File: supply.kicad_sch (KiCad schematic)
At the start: 39 parts, among them IC3 TPS259571DSGR, IC4 BQ27427YZFR, IC4 TPD6E001RSERG4, IC5 MP2722GRH-0000-Z, IC6 TPS62291DRVR, IC7 TPS62293DRVR, J4 UJ20-C-V-SMT-TR-68, J5 SM03B-SRSS-TB_LF__SN_

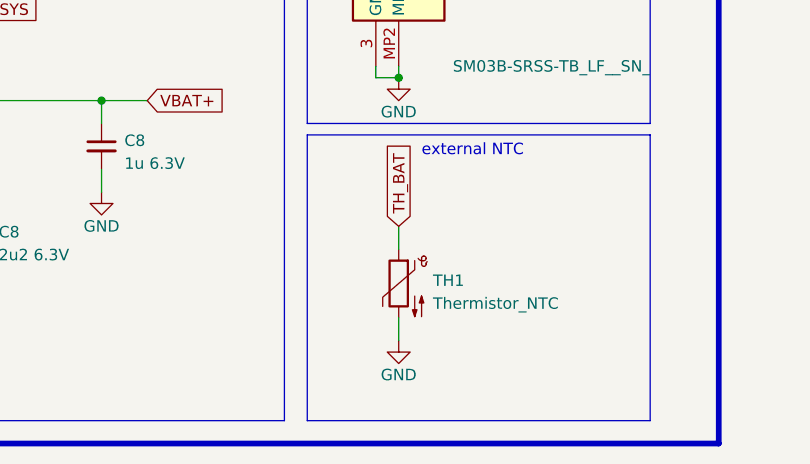
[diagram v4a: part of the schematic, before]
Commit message: first layout iteration
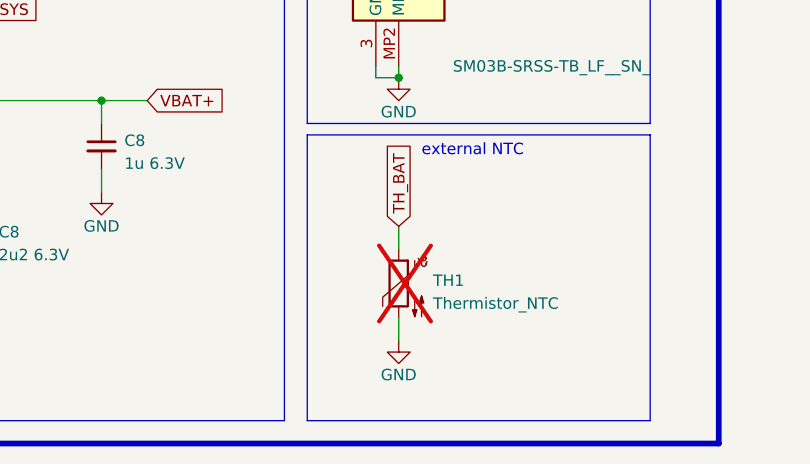
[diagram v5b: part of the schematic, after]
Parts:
- R2: footprint Resistor_SMD:R_0201_0603Metric_Pad0.64x0.40mm_HandSolder -> Resistor_SMD:R_0201_0603Metric
- TH1: now not fitted
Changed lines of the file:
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@@
       (effects (font (size 1.27 1.27)) (justify right))
     )
-    (property "Footprint" "Resistor_SMD:R_0201_0603Metric_Pad0.64x0.40mm_HandSolder" (at 180.34 165.1 0)
+    (property "Footprint" "Resistor_SMD:R_0201_0603Metric" (at 180.34 165.1 0)
       (effects (font (size 1.27 1.27)) hide)
     )
@@
   )
   (symbol (lib_id "Device:Thermistor_NTC") (at 259.08 259.08 0) (mirror y) (unit 1)
-    (in_bom yes) (on_board yes) (dnp no)
+    (in_bom yes) (on_board no) (dnp yes)
     (property "Reference" "TH1" (at 262.89 258.7625 0)
       (effects (font (size 1.27 1.27)) (justify right))

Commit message: progressed layout, adjusted some courtyard sized to be smaller
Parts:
- IC4: Manufacturer_Name (none) -> Texas Instruments; Manufacturer_Part_Number (none) -> TPD6E001RSERG4; Mouser Part Number (none) -> 595-TPD6E001RSERG4; Mouser Price/Stock (none) -> https://www.mouser.co.uk/ProductDetail/Texas-Instruments/TP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
- J4: Manufacturer_Name (none) -> CUI Devices; Manufacturer_Part_Number (none) -> UJ20-C-V-SMT-TR-68; Mouser Part Number (none) -> 179-UJ20-C-V-SMTTR68; Mouser Price/Stock (none) -> https://www.mouser.co.uk/ProductDetail/CUI-Devices/UJ20-C-V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
- R3: footprint Resistor_SMD:R_0201_0603Metric_Pad0.64x0.40mm_HandSolder -> Resistor_SMD:R_0201_0603Metric
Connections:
- net EP: now also J4.B12 (GND_4)
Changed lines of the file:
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@@
       (effects (font (size 1.27 1.27)) (justify right))
     )
-    (property "Footprint" "Resistor_SMD:R_0201_0603Metric_Pad0.64x0.40mm_HandSolder" (at 240.03 40.64 0)
+    (property "Footprint" "Resistor_SMD:R_0201_0603Metric" (at 240.03 40.64 0)
       (effects (font (size 1.27 1.27)) hide)
     )
@@
     (property "MFN" "179-UJ20-C-V-SMTTR68" (at 55.88 46.99 0)
       (effects (font (size 1.27 1.27)) hide)
+    )
+    (property "Mouser Part Number" "179-UJ20-C-V-SMTTR68" (at 26.67 541.91 0)
+      (effects (font (size 1.27 1.27)) (justify left top) hide)
+    )
+    (property "Mouser Price/Stock" "https://www.mouser.co.uk/ProductDetail/CUI-Devices/UJ20-C-V-SMT-TR-68?qs=HoCaDK9Nz5dJB%252B3Mk1F%2F5A%3D%3D" (at 26.67 641.91 0)
+      (effects (font (size 1.27 1.27)) (justify left top) hide)
+    )
+    (property "Manufacturer_Name" "CUI Devices" (at 26.67 741.91 0)
+      (effects (font (size 1.27 1.27)) (justify left top) hide)
+    )
+    (property "Manufacturer_Part_Number" "UJ20-C-V-SMT-TR-68" (at 26.67 841.91 0)
+      (effects (font (size 1.27 1.27)) (justify left top) hide)
     )
     (pin "A1")
@@
       (effects (font (size 1.27 1.27)) hide)
     )
-    (pin "1")
+    (property "Mouser Part Number" "595-TPD6E001RSERG4" (at 134.62 541.91 0)
+      (effects (font (size 1.27 1.27)) (justify left top) hide)
+    )
+    (property "Mouser Price/Stock" "https://www.mouser.co.uk/ProductDetail/Texas-Instruments/TPD6E001RSERG4?qs=t6sYTo5dwUw0xcflr5hU2g%3D%3D" (at 134.62 641.91 0)
+      (effects (font (size 1.27 1.27)) (justify left top) hide)
+    )
+    (property "Manufacturer_Name" "Texas Instruments" (at 134.62 741.91 0)
+      (effects (font (size 1.27 1.27)) (justify left top) hide)
+    )
+    (property "Manufacturer_Part_Number" "TPD6E001RSERG4" (at 134.62 841.91 0)
+      (effects (font (size 1.27 1.27)) (justify left top) hide)
+    )
+    (pin "1")

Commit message: added test points
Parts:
- added TP1 (x11): TestPoint, TestPoint:TestPoint_Pad_D1.0mm, symbol Connector:TestPoint
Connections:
- net +1V8: now also TP1.1
- net +3V3: now also TP1.1
- net EP: now also TP1.1, TP1.1, TP1.1, TP1.1, TP1.1
- net VBAT+: now also TP1.1
- net VSYS: now also TP1.1
- net VUSB: now also TP1.1
- net at C8.1, IC3.3 (IN_1), IC3.4 (IN_2)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: now also TP1.1
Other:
- moved on the sheet: C8, R3

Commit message: Added LED
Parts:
- D1: footprint (none) -> ARMband:LEDC1608X80N; MFN 755-SML-P12YTT86RR -> 710-150060GS75000
- D2: footprint (none) -> ARMband:LEDC1608X80N; MFN 755-SML-P12YTT86RR -> 710-150060SS75003
- R15, R16: footprint (none) -> Resistor_SMD:R_0201_0603Metric
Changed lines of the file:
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@@
       (effects (font (size 1.27 1.27)))
     )
-    (property "Footprint" "" (at 260.35 177.8 0)
+    (property "Footprint" "Resistor_SMD:R_0201_0603Metric" (at 260.35 177.8 0)
       (effects (font (size 1.27 1.27)) hide)
     )
@@
       (effects (font (size 1.27 1.27)))
     )
-    (property "Footprint" "" (at 260.35 182.88 0)
+    (property "Footprint" "Resistor_SMD:R_0201_0603Metric" (at 260.35 182.88 0)
       (effects (font (size 1.27 1.27)) hide)
     )
@@
       (effects (font (size 1.27 1.27)))
     )
-    (property "Footprint" "" (at 242.57 182.88 90)
-      (effects (font (size 1.27 1.27)) hide)
-    )
-    (property "Datasheet" "https://www.mouser.de/datasheet/2/348/rohm_semiconductor_rohm-s-a0008001703-1-1758187.pdf" (at 242.57 182.88 90)
-      (effects (font (size 1.27 1.27)) hide)
-    )
-    (property "MFN" "755-SML-P12YTT86RR" (at 242.57 182.88 0)
+    (property "Footprint" "ARMband:LEDC1608X80N" (at 242.57 182.88 90)
+      (effects (font (size 1.27 1.27)) hide)
+    )
+    (property "Datasheet" "https://www.we-online.com/components/products/datasheet/150060SS75003.pdf" (at 242.57 182.88 90)
+      (effects (font (size 1.27 1.27)) hide)
+    )
+    (property "MFN" "710-150060SS75003" (at 242.57 182.88 0)
       (effects (font (size 1.27 1.27)) hide)
     )
@@
       (effects (font (size 1.27 1.27)))
     )
-    (property "Footprint" "" (at 242.57 177.8 90)
-      (effects (font (size 1.27 1.27)) hide)
-    )
-    (property "Datasheet" "https://www.mouser.de/datasheet/2/348/rohm_semiconductor_rohm-s-a0008001703-1-1758187.pdf" (at 242.57 177.8 90)
-      (effects (font (size 1.27 1.27)) hide)
-    )
-    (property "MFN" "755-SML-P12YTT86RR" (at 242.57 177.8 0)
-      (effects (font (size 1.27 1.27)) hide)
-    )
+    (property "Footprint" "ARMband:LEDC1608X80N" (at 242.57 177.8 90)
+      (effects (font (size 1.27 1.27)) hide)
+    )
+    (property "Datasheet" "https://www.we-online.com/components/products/datasheet/150060GS75000.pdf" (at 242.57 177.8 90)
+      (effects (font (size 1.27 1.27)) hide)
+    )
+    (property "MFN" "710-150060GS75000" (at 242.57 177.8 0)
+      (effects (font (size 1.27 1.27)) hide)
+    )
